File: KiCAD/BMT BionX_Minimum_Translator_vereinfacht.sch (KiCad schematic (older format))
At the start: 28 parts, among them J1 Kunteng LCDx Display Connector, J2 SAE Power Connector Motor, J3 Rosenberg Motor, J4 External BB Torquesensor, J5 Brake connector, J6 Throttle connector, J7 CAN Connector, J9 Batterieanschluß, Q1 IRF3205, Q2 IRF3205, U1 BP, U2 MCP2551-CAN Transceiver, U3 VOM1271, U4 SD12-5

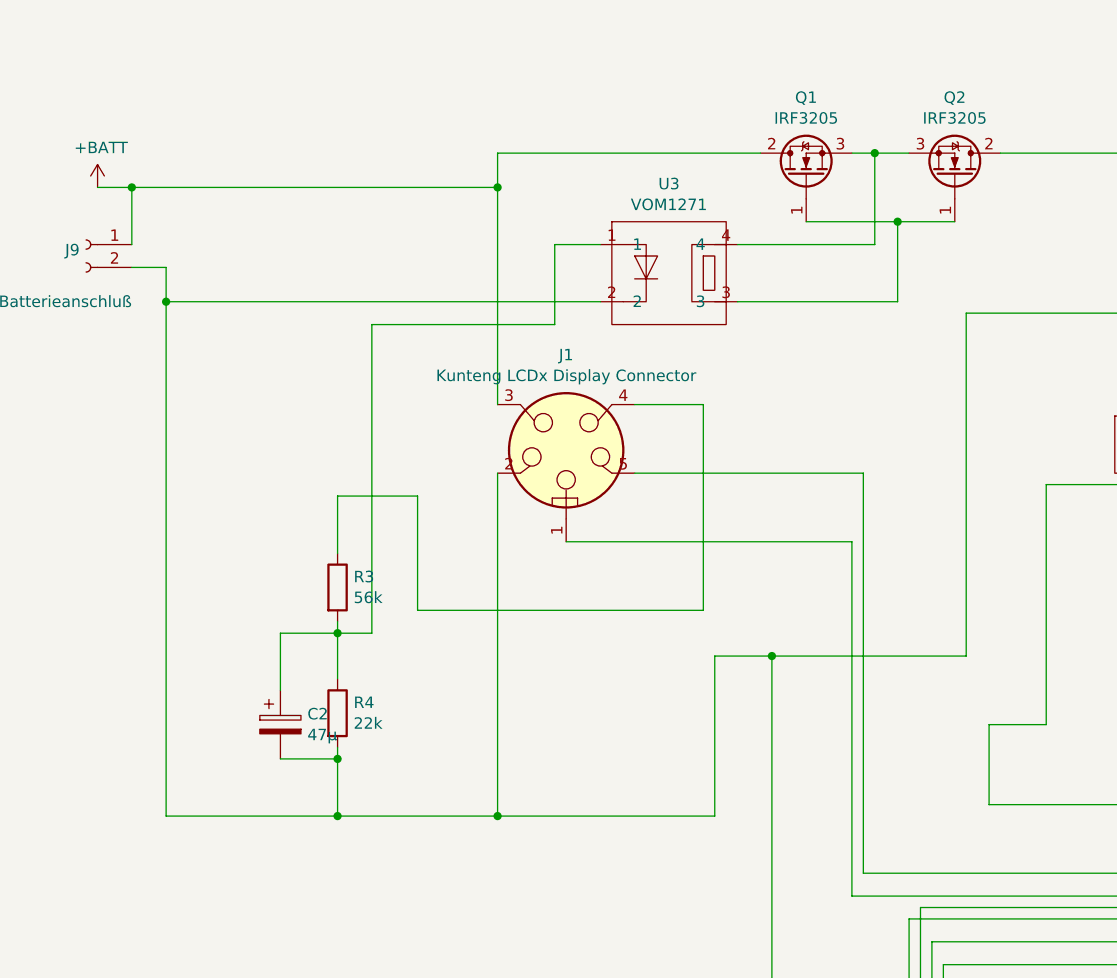
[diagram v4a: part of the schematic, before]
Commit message: switched to 0805 Size
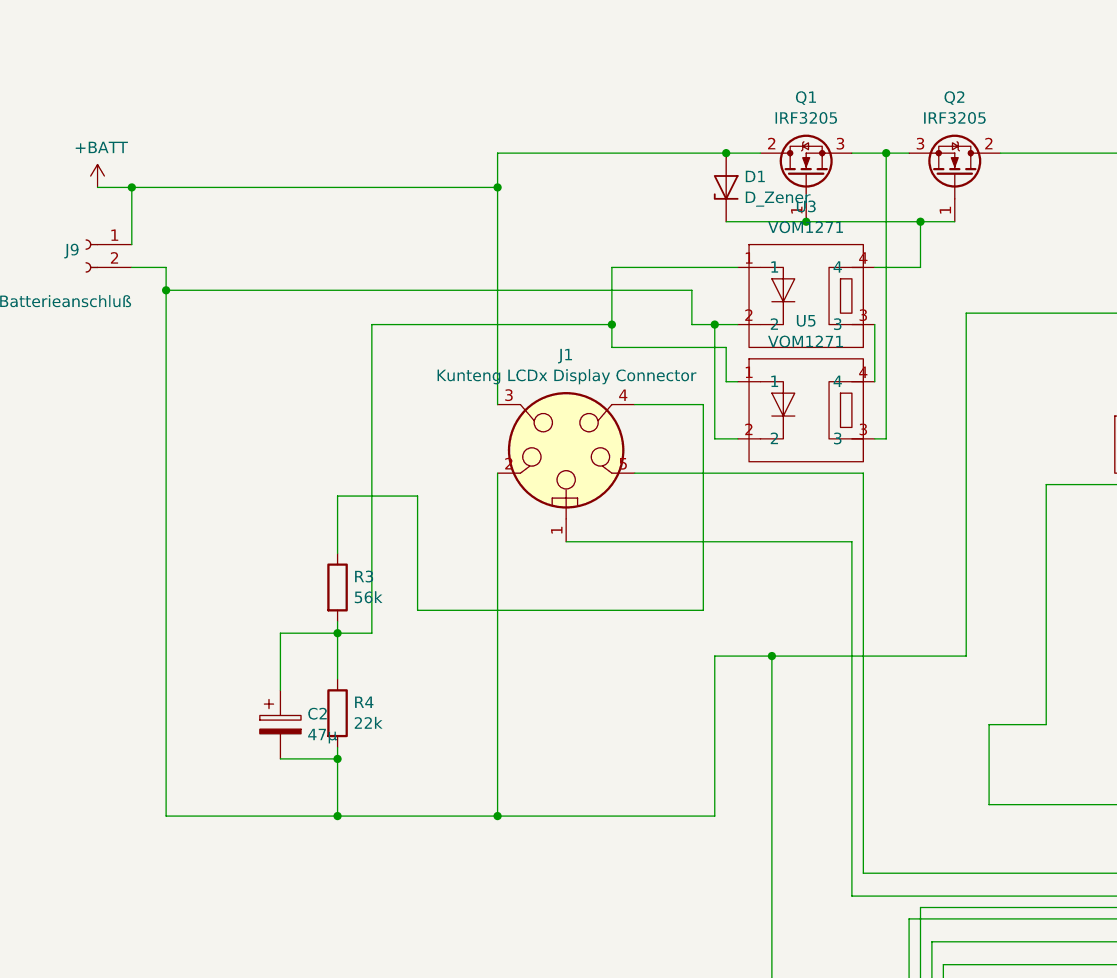
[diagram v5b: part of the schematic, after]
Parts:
- added D1: D_Zener, Diode_SMD:D_0805_2012Metric, symbol Device:D_Zener
- added U5: VOM1271, Package_SO:SOP-4_3.8x4.1mm_P2.54mm, symbol Driver_FET:VOM1271
- R1, R10, R2, R3, R4, R5, R6, R7, R8: footprint Resistor_SMD:R_2512_6332Metric -> Resistor_SMD:R_0805_2012Metric
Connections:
- net +BATT: now also D1.2 (A)
- net GND: now also U5.2
- net at C2.1, R3.2, R4.1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: now also U5.1
- net at Q1.1 (G), Q2.1 (G): now also U3.4, D1.1 (K); no longer U3.3
- net at Q1.3 (S), Q2.3 (S): now also U5.3; no longer U3.4
- new net: U3.3, U5.4
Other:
- moved on the sheet: U3
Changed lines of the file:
@@
 F 0 "R3" H 2120 3396 50  0000 L CNN
 F 1 "56k" H 2120 3305 50  0000 L CNN
-F 2 "Resistor_SMD:R_2512_6332Metric" V 1980 3350 50  0001 C CNN
+F 2 "Resistor_SMD:R_0805_2012Metric" V 1980 3350 50  0001 C CNN
 F 3 "~" H 2050 3350 50  0001 C CNN
 	1    2050 3350
@@
 F 0 "R4" H 2120 3946 50  0000 L CNN
 F 1 "22k" H 2120 3855 50  0000 L CNN
-F 2 "Resistor_SMD:R_2512_6332Metric" V 1980 3900 50  0001 C CNN
+F 2 "Resistor_SMD:R_0805_2012Metric" V 1980 3900 50  0001 C CNN
 F 3 "~" H 2050 3900 50  0001 C CNN
 	1    2050 3900
@@
 	2400 3450 3650 3450
 Wire Wire Line
-	2200 2200 3000 2200
-Wire Wire Line
 	2200 2200 2200 3550
 Wire Wire Line
@@
 F 0 "R8" H 9120 4896 50  0000 L CNN
 F 1 "2.2k" H 9120 4805 50  0000 L CNN
-F 2 "Resistor_SMD:R_2512_6332Metric" V 8980 4850 50  0001 C CNN
+F 2 "Resistor_SMD:R_0805_2012Metric" V 8980 4850 50  0001 C CNN
 F 3 "~" H 9050 4850 50  0001 C CNN
 	1    9050 4850
@@
 F 0 "R7" H 9120 4446 50  0000 L CNN
 F 1 "1k" H 9120 4355 50  0000 L CNN
-F 2 "Resistor_SMD:R_2512_6332Metric" V 8980 4400 50  0001 C CNN
+F 2 "Resistor_SMD:R_0805_2012Metric" V 8980 4400 50  0001 C CNN
 F 3 "~" H 9050 4400 50  0001 C CNN
 	1    9050 4400
@@
 F 0 "R6" H 6720 2396 50  0000 L CNN
 F 1 "2.2k" H 6720 2305 50  0000 L CNN
-F 2 "Resistor_SMD:R_2512_6332Metric" V 6580 2350 50  0001 C CNN
+F 2 "Resistor_SMD:R_0805_2012Metric" V 6580 2350 50  0001 C CNN
 F 3 "~" H 6650 2350 50  0001 C CNN
 	1    6650 2350
@@
 	2050 4350 1300 4350
 Wire Wire Line
-	1300 4350 1300 2100
-Wire Wire Line
 	1300 1950 1150 1950
 Connection ~ 2050 4350
@@
 $EndComp
 Wire Wire Line
-	4300 1450 4400 1450
-Wire Wire Line
 	7700 1450 7700 950
 Wire Wire Line
 	2750 1600 2750 1450
 Wire Wire Line
-	2750 1450 3900 1450
+	2750 1450 3750 1450
 Connection ~ 2750 1600
-Wire Wire Line
-	4100 1750 4500 1750
 $Comp
 L Driver_FET:VOM1271 U3
 U 1 1 5F894B49
-P 3500 1600
-F 0 "U3" H 3500 1615 50  0000 C CNN
-F 1 "VOM1271" H 3500 1524 50  0000 C CNN
-F 2 "Package_SO:SOP-4_3.8x4.1mm_P2.54mm" H 3500 1600 50  0001 C CNN
-F 3 "" H 3500 1600 50  0001 C CNN
-	1    3500 1600
-	1    0    0    -1
-$EndComp
-Wire Wire Line
-	3000 1850 3200 1850
-Wire Wire Line
-	3000 1850 3000 2200
-Wire Wire Line
-	1300 2100 3200 2100
-Connection ~ 1300 2100
-Wire Wire Line
-	1300 2100 1300 1950
-Wire Wire Line
-	3800 1850 4400 1850
-Wire Wire Line
-	4400 1850 4400 1450
-Connection ~ 4400 1450
-Wire Wire Line
-	4400 1450 4550 1450
-Wire Wire Line
-	4500 1750 4500 2100
-Wire Wire Line
-	4500 2100 3800 2100
-Connection ~ 4500 1750
-Wire Wire Line
-	4500 1750 4750 1750
+P 4100 1700
+F 0 "U3" H 4100 1715 50  0000 C CNN
+F 1 "VOM1271" H 4100 1624 50  0000 C CNN
+F 2 "Package_SO:SOP-4_3.8x4.1mm_P2.54mm" H 4100 1700 50  0001 C CNN
+F 3 "" H 4100 1700 50  0001 C CNN
+	1    4100 1700
+	1    0    0    -1
+$EndComp
 $Comp
 L Device:CP C1
@@
 F 0 "R1" H 7570 2946 50  0000 L CNN
 F 1 "2.2k" H 7570 2855 50  0000 L CNN
-F 2 "Resistor_SMD:R_2512_6332Metric" V 7430 2900 50  0001 C CNN
+F 2 "Resistor_SMD:R_0805_2012Metric" V 7430 2900 50  0001 C CNN
 F 3 "~" H 7500 2900 50  0001 C CNN
 	1    7500 2900
@@
 F 0 "R2" H 7720 2346 50  0000 L CNN
 F 1 "2.2k" H 7720 2255 50  0000 L CNN
-F 2 "Resistor_SMD:R_2512_6332Metric" V 7580 2300 50  0001 C CNN
+F 2 "Resistor_SMD:R_0805_2012Metric" V 7580 2300 50  0001 C CNN
 F 3 "~" H 7650 2300 50  0001 C CNN
 	1    7650 2300
@@
 F 0 "R10" H 7270 6196 50  0000 L CNN
 F 1 "10k" H 7270 6105 50  0000 L CNN
-F 2 "Resistor_SMD:R_2512_6332Metric" V 7130 6150 50  0001 C CNN
+F 2 "Resistor_SMD:R_0805_2012Metric" V 7130 6150 50  0001 C CNN
 F 3 "~" H 7200 6150 50  0001 C CNN
 	1    7200 6150
@@
 F 0 "R5" H 6720 1946 50  0000 L CNN
 F 1 "1k" H 6720 1855 50  0000 L CNN
-F 2 "Resistor_SMD:R_2512_6332Metric" V 6580 1900 50  0001 C CNN
+F 2 "Resistor_SMD:R_0805_2012Metric" V 6580 1900 50  0001 C CNN
 F 3 "~" H 6650 1900 50  0001 C CNN
 	1    6650 1900
@@
 Wire Wire Line
 	5150 2900 5150 3950
+$Comp
+L Driver_FET:VOM1271 U5
+U 1 1 5F86ABF3
+P 4100 2200
+F 0 "U5" H 4100 2215 50  0000 C CNN
+F 1 "VOM1271" H 4100 2124 50  0000 C CNN
+F 2 "Package_SO:SOP-4_3.8x4.1mm_P2.54mm" H 4100 2200 50  0001 C CNN
+F 3 "" H 4100 2200 50  0001 C CNN
+	1    4100 2200
+	1    0    0    -1
+$EndComp
+Wire Wire Line
+	3750 2450 3800 2450
+Wire Wire Line
+	1300 1950 1300 2050
+Wire Wire Line
+	4300 1450 4450 1450
+Wire Wire Line
+	3250 2200 3250 1950
+Wire Wire Line
+	3250 1950 3800 1950
+Wire Wire Line
+	2200 2200 3250 2200
+Wire Wire Line
+	3250 2200 3250 2300
+Wire Wire Line
+	3250 2300 3750 2300
+Wire Wire Line
+	3750 2300 3750 2450
+Connection ~ 3250 2200
+Wire Wire Line
+	1300 2050 3600 2050
+Wire Wire Line
+	3600 2050 3600 2200
+Wire Wire Line
+	3600 2200 3700 2200
+Connection ~ 1300 2050
+Wire Wire Line
+	1300 2050 1300 4350
+Wire Wire Line
+	3700 2200 3700 2700
+Wire Wire Line
+	3700 2700 3800 2700
+Connection ~ 3700 2200
+Wire Wire Line
+	3700 2200 3800 2200
+Wire Wire Line
+	4400 2450 4400 2200
+Wire Wire Line
+	4400 1950 4600 1950
+Wire Wire Line
+	4600 1950 4600 1750
+Connection ~ 4600 1750
+Wire Wire Line
+	4600 1750 4750 1750
+Wire Wire Line
+	4400 2700 4450 2700
+Wire Wire Line
+	4450 2700 4450 1450
+Connection ~ 4450 1450
+Wire Wire Line
+	4450 1450 4550 1450
+$Comp
+L Device:D_Zener D1
+U 1 1 5F8D8CD0
+P 3750 1600
+F 0 "D1" V 3796 1521 50  0000 R CNN
+F 1 "D_Zener" V 3705 1521 50  0000 R CNN
+F 2 "Diode_SMD:D_0805_2012Metric" H 3750 1600 50  0001 C CNN
+F 3 "~" H 3750 1600 50  0001 C CNN
+	1    3750 1600
+	0    -1   -1   0
+$EndComp
+Connection ~ 3750 1450
+Wire Wire Line
+	3750 1450 3900 1450
+Wire Wire Line
+	3750 1750 4100 1750
+Connection ~ 4100 1750
+Wire Wire Line
+	4100 1750 4600 1750
 $EndSCHEMATC

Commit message: schematic as pdf updated
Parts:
- D1: value D_Zener -> 15V
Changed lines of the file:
@@
 P 3750 1600
 F 0 "D1" V 3796 1521 50  0000 R CNN
-F 1 "D_Zener" V 3705 1521 50  0000 R CNN
+F 1 "15V" V 3705 1521 50  0000 R CNN
 F 2 "Diode_SMD:D_0805_2012Metric" H 3750 1600 50  0001 C CNN
 F 3 "~" H 3750 1600 50  0001 C CNN

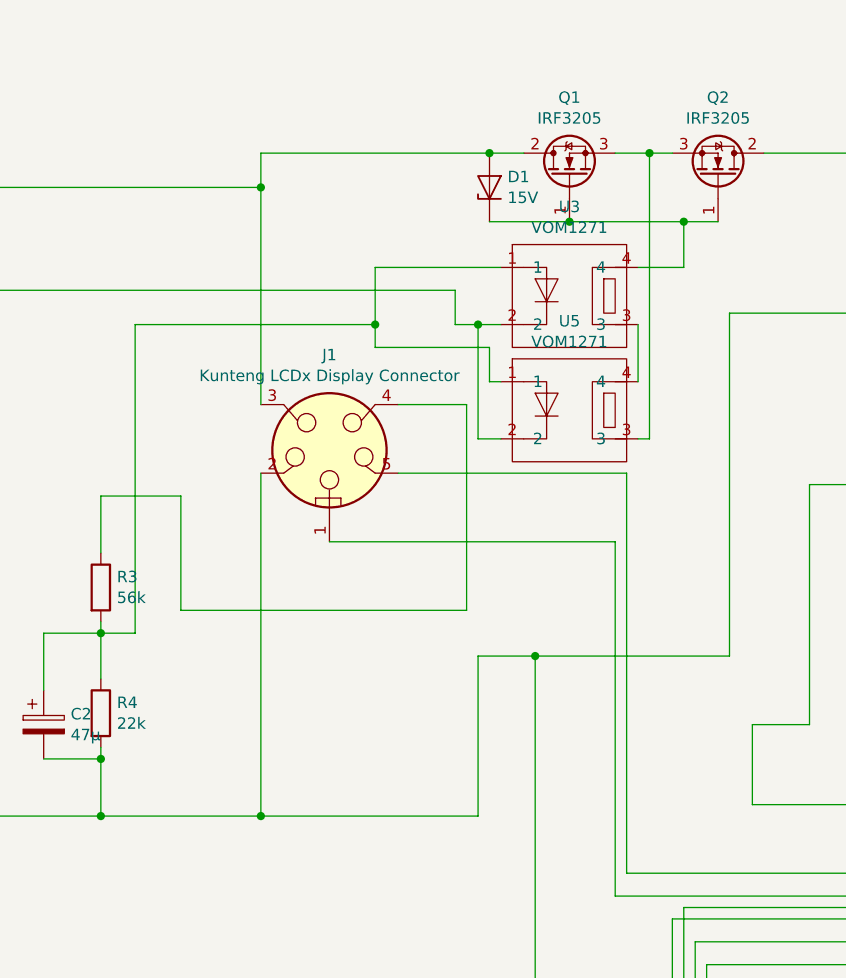
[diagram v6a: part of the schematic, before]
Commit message: 2 Layer routing
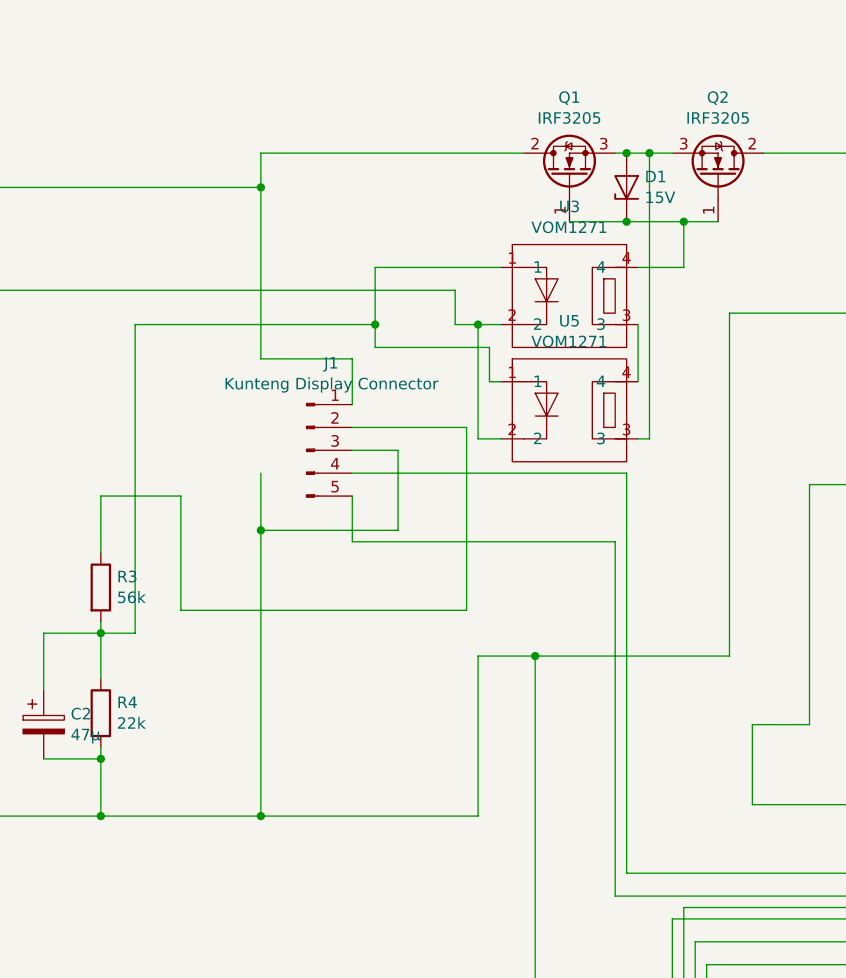
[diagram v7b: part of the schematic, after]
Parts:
- removed J1: Kunteng LCDx Display Connector, Connector_JST:JST_EH_B5B-EH-A_1x05_P2.50mm_Vertical, symbol Connector:LEMO5
- added J1: Kunteng Display Connector, Connector_JST:JST_EH_B5B-EH-A_1x05_P2.50mm_Vertical, symbol Connector:Conn_01x05_Male
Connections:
- net +BATT: now also J1.1 (Pin_1); no longer D1.2 (A)
- net GND: now also J1.3 (Pin_3)
- net at U1.PA10: now also J1.5 (Pin_5)
- net at R3.1: now also J1.2 (Pin_2)
- net at U1.PA9: now also J1.4 (Pin_4)
- net at Q1.3 (S), Q2.3 (S), U5.3: now also D1.2 (A)
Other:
- moved on the sheet: D1
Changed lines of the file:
@@
 	1    0    0    -1
 $EndComp
-$Comp
-L Connector:LEMO5 J1
-U 1 1 5F23DDCC
-P 3050 2750
-F 0 "J1" H 3050 3167 50  0000 C CNN
-F 1 "Kunteng LCDx Display Connector" H 3050 3076 50  0000 C CNN
-F 2 "Connector_JST:JST_EH_B5B-EH-A_1x05_P2.50mm_Vertical" H 3050 2750 50  0001 C CNN
-F 3 " ~" H 3050 2750 50  0001 C CNN
-	1    3050 2750
-	1    0    0    -1
-$EndComp
-Wire Wire Line
-	2750 4350 2750 2850
-Wire Wire Line
-	2750 1600 2750 2550
+Wire Wire Line
+	2750 4350 2750 3100
+Wire Wire Line
+	2750 1600 2750 2350
 $Comp
 L Device:R R3
@@
 	1    0    0    -1
 $EndComp
-Wire Wire Line
-	3350 2550 3650 2550
-Wire Wire Line
-	3650 2550 3650 3450
 Wire Wire Line
 	2050 3500 2050 3550
@@
 	6500 2750 7500 2750
 Wire Wire Line
-	3350 2850 4350 2850
-Wire Wire Line
-	4350 2850 4350 4600
-Wire Wire Line
 	4350 4600 6650 4600
 Wire Wire Line
@@
 Wire Wire Line
 	6650 6500 6250 6500
-Wire Wire Line
-	3050 3150 4300 3150
 Wire Wire Line
 	4300 3150 4300 4700
@@
 Wire Wire Line
 	2750 1600 2750 1450
-Wire Wire Line
-	2750 1450 3750 1450
 Connection ~ 2750 1600
 $Comp
@@
 	1300 1950 1300 2050
 Wire Wire Line
-	4300 1450 4450 1450
+	4300 1450 4350 1450
 Wire Wire Line
 	3250 2200 3250 1950
@@
 L Device:D_Zener D1
 U 1 1 5F8D8CD0
-P 3750 1600
-F 0 "D1" V 3796 1521 50  0000 R CNN
-F 1 "15V" V 3705 1521 50  0000 R CNN
-F 2 "Diode_SMD:D_0805_2012Metric" H 3750 1600 50  0001 C CNN
-F 3 "~" H 3750 1600 50  0001 C CNN
-	1    3750 1600
+P 4350 1600
+F 0 "D1" V 4396 1521 50  0000 R CNN
+F 1 "15V" V 4305 1521 50  0000 R CNN
+F 2 "Diode_SMD:D_0805_2012Metric" H 4350 1600 50  0001 C CNN
+F 3 "~" H 4350 1600 50  0001 C CNN
+	1    4350 1600
 	0    -1   -1   0
 $EndComp
-Connection ~ 3750 1450
-Wire Wire Line
-	3750 1450 3900 1450
-Wire Wire Line
-	3750 1750 4100 1750
-Connection ~ 4100 1750
-Wire Wire Line
-	4100 1750 4600 1750
+Wire Wire Line
+	4100 1750 4350 1750
+$Comp
+L Connector:Conn_01x05_Male J1
+U 1 1 5F8510AE
+P 2950 2750
+F 0 "J1" H 3058 3131 50  0000 C CNN
+F 1 "Kunteng Display Connector" H 3058 3040 50  0000 C CNN
+F 2 "Connector_JST:JST_EH_B5B-EH-A_1x05_P2.50mm_Vertical" H 2950 2750 50  0001 C CNN
+F 3 "~" H 2950 2750 50  0001 C CNN
+	1    2950 2750
+	1    0    0    -1
+$EndComp
+Wire Wire Line
+	2750 2350 3150 2350
+Wire Wire Line
+	3150 2350 3150 2550
+Wire Wire Line
+	3150 2650 3650 2650
+Wire Wire Line
+	3650 2650 3650 3450
+Wire Wire Line
+	2750 3100 3350 3100
+Wire Wire Line
+	3350 2750 3150 2750
+Connection ~ 2750 3100
+Wire Wire Line
+	2750 3100 2750 2850
+Wire Wire Line
+	3350 2750 3350 3100
+Wire Wire Line
+	3150 3150 3150 2950
+Wire Wire Line
+	3150 3150 4300 3150
+Wire Wire Line
+	4350 2850 4350 4600
+Wire Wire Line
+	3150 2850 4350 2850
+Connection ~ 4350 1750
+Wire Wire Line
+	4350 1750 4600 1750
+Connection ~ 4350 1450
+Wire Wire Line
+	4350 1450 4450 1450
+Wire Wire Line
+	2750 1450 3900 1450
 $EndSCHEMATC
